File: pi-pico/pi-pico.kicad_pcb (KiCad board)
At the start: 2 copper layers, 124 x 44 mm, 32 parts, among them J1 BT A, J10 ENC L, J11 ENC R, J2 BT B, J3 BT C, J4 BT D, J5 FX L, J6 FX R, J7 Start, J8 POT L, J9 POT R, Q1 BSS138, Q2 BSS138, Q3 BSS138, Q4 BSS138, Q5 BSS138, Q6 BSS138, Q7 BSS138, SW1 SW_DIP_x01

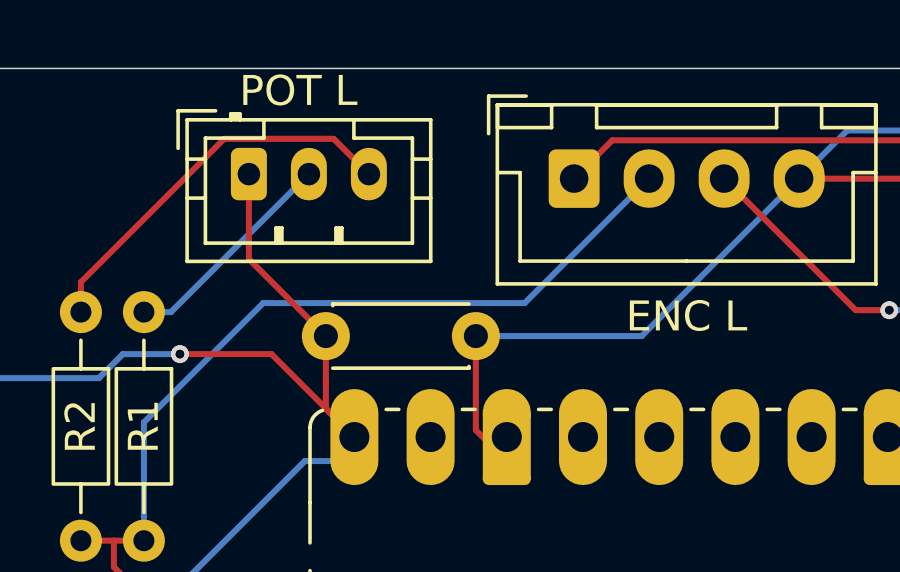
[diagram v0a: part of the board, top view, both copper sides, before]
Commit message: Fix right mosfets not connected to 5V
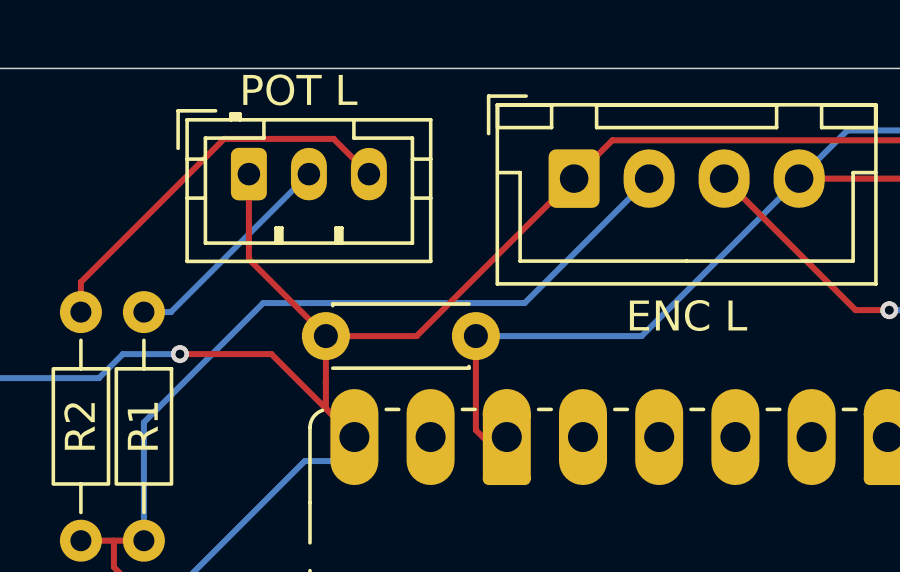
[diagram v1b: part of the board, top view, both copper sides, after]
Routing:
- net +5V: track 167.5 -> 178.0 mm
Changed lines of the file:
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@@
+	)
+	(segment
+		(start 130.091 80.899)
+		(end 135.3404 75.6496)
+		(width 0.2)
+		(layer "F.Cu")
+		(net 16)
 	)
 	(segment
@@
 		(width 0.2)
 		(layer "F.Cu")
+		(net 16)
+	)
+	(segment
+		(start 127.0654 80.899)
+		(end 130.091 80.899)
+		(width 0.2)
+		(layer "F.Cu")

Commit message: Complete refactor: V4
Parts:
- removed J8: POT L, Connector_JST:JST_PH_B3B-PH-K_1x03_P2.00mm_Vertical
- removed J9: POT R, Connector_JST:JST_PH_B3B-PH-K_1x03_P2.00mm_Vertical
- removed Q1: BSS138, Package_TO_SOT_SMD:SOT-23
- removed R1, R3: 1k, Resistor_THT:R_Axial_DIN0204_L3.6mm_D1.6mm_P7.62mm_Horizontal
- removed R2, R4: 2k, Resistor_THT:R_Axial_DIN0204_L3.6mm_D1.6mm_P7.62mm_Horizontal
- removed SW1: SW_DIP_x01, Button_Switch_SMD:SW_DIP_SPSTx01_Slide_9.78x4.72mm_W8.61mm_P2.54mm
- added Q8: BSS138, Package_TO_SOT_SMD:SOT-23, F.Cu at (196.0, 106.2)
- moved Q3 62.1 mm to (123.2, 106.2)
- moved Q7 59.2 mm to (181.5, 106.2)
- moved Q4 55.4 mm to (138.0, 106.2)
- moved Q5 38.5 mm to (152.2, 106.0)
- moved Q6 22.4 mm to (167.0, 106.2)
- moved J11 21.3 mm to (185.2, 75.7)
- moved J10 17.6 mm to (117.8, 76.0)
- moved Q2 8.95 mm to (109.2, 106.2)
- moved C1 5.38 mm to (131.8, 78.2)
- moved A1 4.54 mm to (155.9, 91.4)
- moved R5 2.24 mm to (110.2, 84.4)
- moved R6 2.24 mm to (107.2, 84.4)
- moved USB1 2.00 mm to (109.0, 70.7)
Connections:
- net Net-(A1-GPIO0) renamed BT-A
- net Net-(A1-GPIO1) renamed FX-L
- net Net-(A1-GPIO2) renamed BT-B
- net Net-(A1-GPIO3) renamed START
- net Net-(A1-GPIO4) renamed BT-C
- net Net-(A1-GPIO5) renamed FX-R
- net Net-(A1-GPIO6) renamed BT-D
- A1 pad 26: Net-(A1-GPIO20) -> unconnected-(A1-GPIO20-Pad26)
- J1 pad 2: GND -> BT-A LED
- J1 pad 3: BT-A LED -> +5V
- J2 pad 2: GND -> BT-B LED
- J2 pad 3: BT-B LED -> +5V
- J3 pad 2: GND -> BT-C LED
- J3 pad 3: BT-C LED -> +5V
- J4 pad 2: GND -> BT-D LED
- J4 pad 3: BT-D LED -> +5V
- J5 pad 2: GND -> FX-L LED
- J5 pad 3: FX-L LED -> +5V
- J6 pad 2: GND -> FX-R LED
- J6 pad 3: FX-R LED -> +5V
- J7 pad 2: GND -> START LED
- J7 pad 3: START LED -> +5V
- Q2 pad 1: BT-B LED -> Net-(A1-GPIO7)
- Q2 pad 2: Net-(A1-GPIO8) -> BT-A LED
- Q2 pad 3: +5V -> GND
- Q3 pad 1: BT-C LED -> Net-(A1-GPIO8)
- Q3 pad 2: Net-(A1-GPIO13) -> FX-L LED
- Q3 pad 3: +5V -> GND
- Q4 pad 1: BT-D LED -> Net-(A1-GPIO9)
- Q4 pad 2: Net-(A1-GPIO11) -> BT-B LED
- Q4 pad 3: +5V -> GND
- Q5 pad 1: FX-L LED -> Net-(A1-GPIO10)
- Q5 pad 2: Net-(A1-GPIO9) -> START LED
- Q5 pad 3: +5V -> GND
- Q6 pad 1: FX-R LED -> Net-(A1-GPIO11)
- Q6 pad 2: Net-(A1-GPIO12) -> BT-C LED
- Q6 pad 3: +5V -> GND
- Q7 pad 1: START LED -> Net-(A1-GPIO12)
- Q7 pad 2: Net-(A1-GPIO7) -> FX-R LED
- Q7 pad 3: +5V -> GND
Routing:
- net GND: track 244.0 -> 459.3 mm
- net +5V: track 178.0 -> 264.1 mm, vias 5 -> 2
- net Net-(A1-GPIO10): track 53.3 -> 14.1 mm, vias 0 -> 1
- net Net-(A1-GPIO11): track 36.1 -> 7.46 mm, vias 0 -> 1
- net AGND: track 26.3 -> 0.00 mm
- net START LED: track 32.6 -> 7.09 mm
- net Net-(A1-GPIO16): track 85.5 -> 63.5 mm, vias 2 -> 0
- net Net-(A1-GPIO9): track 43.6 -> 23.3 mm, vias 0 -> 1
- net Net-(J9-Pin_2): track 19.2 -> 0.00 mm
- net Net-(A1-GPIO7): track 29.7 -> 47.0 mm, vias 0 -> 1
- net BT-B LED: track 22.2 -> 6.91 mm
- net Net-(A1-GPIO19): track 10.9 -> 24.8 mm, vias 1 -> 0
- net BT-C LED: track 19.8 -> 6.97 mm
- net Net-(A1-GPIO20): track 10.8 -> 0.00 mm
- net Net-(A1-GPIO18): track 9.84 -> 19.9 mm
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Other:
- board text added: "+5V"
- board text added: "1μF"
- board text added: "LED-"
- board text added: "Minnowboard V4"
- board text removed: "1k"
- board text removed: "2k"
- board text removed: "ENC"
- board text removed: "LED"
- board text removed: "Minnowboard V3"
- board text removed: "OUT"
- board text removed: "POT"
